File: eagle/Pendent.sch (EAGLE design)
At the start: 25 parts, among them Q1 CMA-4544PF-W, U1 Tiny85-20-SMT, U2 LF50ABDT-TR

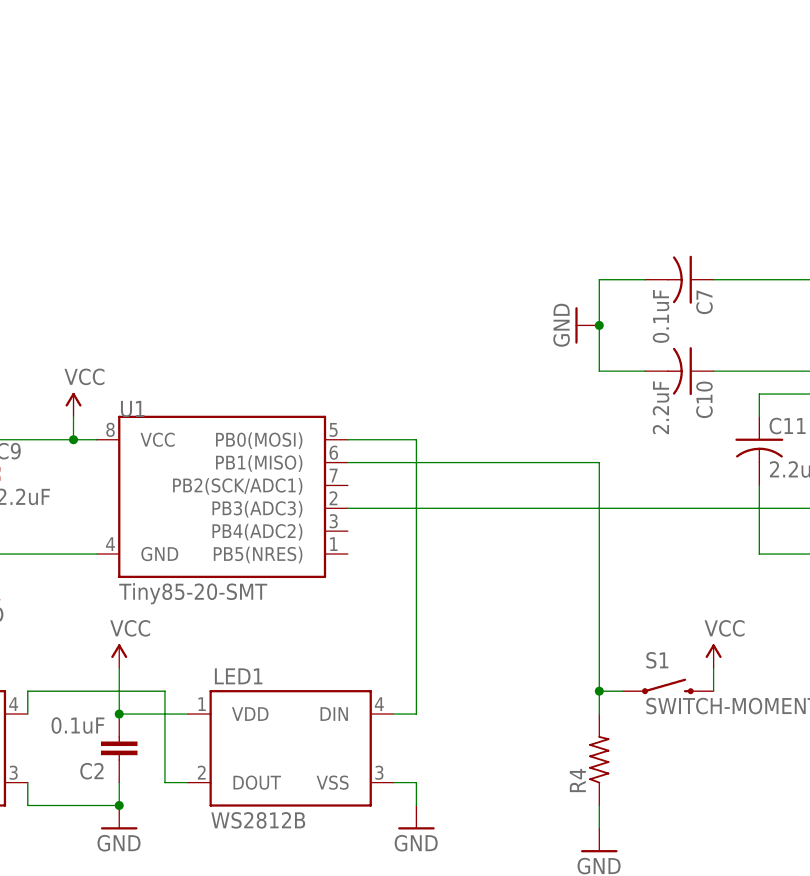
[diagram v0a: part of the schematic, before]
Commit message: Add IRSend add IR LED to schematic
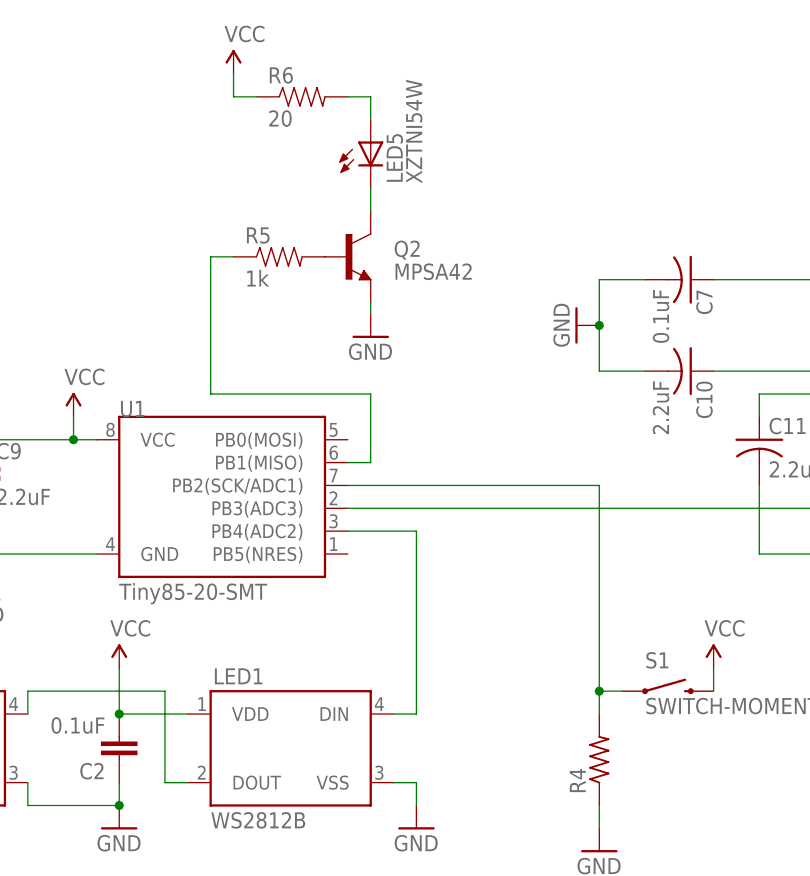
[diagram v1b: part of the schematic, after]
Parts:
- added LED5: XZTNI54W, adafruit:LEDCHIP-LED0805
- added Q2: MPSA42, SparkFun-DiscreteSemi:TRANSISTOR_NPNMPSA42
- added R5: 1k, SparkFun-Passives:RESISTOR0805-RES
- added R6: 20, SparkFun-Passives:RESISTOR0805-RES
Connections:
- new net N$13: Q2.B, R5.2
- new net N$15: LED5.C, Q2.C
- new net N$16: LED5.A, R6.2
- new net N$17: R5.1, U1.PB1(MISO)
- net GND: now also Q2.E
- net N$12: now also U1.PB2(SCK/ADC1); no longer U1.PB1(MISO)
- net N$4: now also U1.PB4(ADC2); no longer U1.PB0(MOSI)
- net VCC: now also R6.1
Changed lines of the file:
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@@
 <part name="GND11" library="SparkFun" deviceset="GND" device=""/>
 <part name="R4" library="adafruit" deviceset="R-US_" device="M0805"/>
+<part name="Q2" library="SparkFun-DiscreteSemi" deviceset="TRANSISTOR_NPN" device="MPSA42" value="MPSA42"/>
+<part name="GND12" library="supply1" deviceset="GND" device=""/>
+<part name="R5" library="SparkFun-Passives" deviceset="RESISTOR" device="0805-RES" value="1k"/>
+<part name="LED5" library="adafruit" deviceset="LED" device="CHIP-LED0805" value="XZTNI54W"/>
+<part name="R6" library="SparkFun-Passives" deviceset="RESISTOR" device="0805-RES" value="20"/>
+<part name="P+8" library="SparkFun" deviceset="VCC" device=""/>
 </parts>
 <sheets>
@@
 <instance part="GND11" gate="1" x="154.94" y="101.6"/>
 <instance part="R4" gate="G$1" x="154.94" y="111.76" rot="R90"/>
+<instance part="Q2" gate="G$1" x="127" y="167.64"/>
+<instance part="GND12" gate="1" x="129.54" y="158.75"/>
+<instance part="R5" gate="G$1" x="119.38" y="167.64"/>
+<instance part="LED5" gate="G$1" x="129.54" y="180.34"/>
+<instance part="R6" gate="G$1" x="121.92" y="185.42"/>
+<instance part="P+8" gate="1" x="114.3" y="187.96"/>
 </instances>
 <busses>
@@
 <pinref part="P+7" gate="1" pin="VCC"/>
 <wire x1="167.64" y1="119.38" x2="167.64" y2="121.92" width="0.1524" layer="91"/>
+</segment>
+<segment>
+<pinref part="P+8" gate="1" pin="VCC"/>
+<wire x1="114.3" y1="187.96" x2="114.3" y2="185.42" width="0.1524" layer="91"/>
+<pinref part="R6" gate="G$1" pin="1"/>
+<wire x1="114.3" y1="185.42" x2="116.84" y2="185.42" width="0.1524" layer="91"/>
 </segment>
 </net>
@@
 <wire x1="154.94" y1="106.68" x2="154.94" y2="104.14" width="0.1524" layer="91"/>
 </segment>
+<segment>
+<pinref part="Q2" gate="G$1" pin="E"/>
+<pinref part="GND12" gate="1" pin="GND"/>
+<wire x1="129.54" y1="161.29" x2="129.54" y2="162.56" width="0.1524" layer="91"/>
+</segment>
 </net>
 <net name="N$1" class="0">
@@
 <net name="N$4" class="0">
 <segment>
-<pinref part="U1" gate="G$1" pin="PB0(MOSI)"/>
-<wire x1="127" y1="147.32" x2="134.62" y2="147.32" width="0.1524" layer="91"/>
-<wire x1="134.62" y1="147.32" x2="134.62" y2="116.84" width="0.1524" layer="91"/>
 <pinref part="LED1" gate="G$1" pin="DIN"/>
+<wire x1="134.62" y1="137.16" x2="134.62" y2="116.84" width="0.1524" layer="91"/>
 <wire x1="134.62" y1="116.84" x2="132.08" y2="116.84" width="0.1524" layer="91"/>
+<pinref part="U1" gate="G$1" pin="PB4(ADC2)"/>
+<wire x1="127" y1="137.16" x2="134.62" y2="137.16" width="0.1524" layer="91"/>
 </segment>
 </net>
@@
 <pinref part="S1" gate="G$1" pin="1"/>
 <wire x1="154.94" y1="119.38" x2="157.48" y2="119.38" width="0.1524" layer="91"/>
-<wire x1="154.94" y1="119.38" x2="154.94" y2="144.78" width="0.1524" layer="91"/>
+<wire x1="154.94" y1="119.38" x2="154.94" y2="142.24" width="0.1524" layer="91"/>
 <junction x="154.94" y="119.38"/>
+<pinref part="U1" gate="G$1" pin="PB2(SCK/ADC1)"/>
+<wire x1="127" y1="142.24" x2="154.94" y2="142.24" width="0.1524" layer="91"/>
+</segment>
+</net>
+<net name="N$13" class="0">
+<segment>
+<pinref part="Q2" gate="G$1" pin="B"/>
+<pinref part="R5" gate="G$1" pin="2"/>
+</segment>
+</net>
+<net name="N$15" class="0">
+<segment>
+<pinref part="Q2" gate="G$1" pin="C"/>
+<pinref part="LED5" gate="G$1" pin="C"/>
+<wire x1="129.54" y1="172.72" x2="129.54" y2="175.26" width="0.1524" layer="91"/>
+</segment>
+</net>
+<net name="N$16" class="0">
+<segment>
+<pinref part="R6" gate="G$1" pin="2"/>
+<wire x1="127" y1="185.42" x2="129.54" y2="185.42" width="0.1524" layer="91"/>
+<pinref part="LED5" gate="G$1" pin="A"/>
+<wire x1="129.54" y1="185.42" x2="129.54" y2="182.88" width="0.1524" layer="91"/>
+</segment>
+</net>
+<net name="N$17" class="0">
+<segment>
 <pinref part="U1" gate="G$1" pin="PB1(MISO)"/>
-<wire x1="154.94" y1="144.78" x2="127" y2="144.78" width="0.1524" layer="91"/>
-</segment>
-</net>
+<wire x1="127" y1="144.78" x2="129.54" y2="144.78" width="0.1524" layer="91"/>
+<wire x1="129.54" y1="144.78" x2="129.54" y2="152.4" width="0.1524" layer="91"/>
+<wire x1="129.54" y1="152.4" x2="111.76" y2="152.4" width="0.1524" layer="91"/>
+<wire x1="111.76" y1="152.4" x2="111.76" y2="167.64" width="0.1524" layer="91"/>
+<pinref part="R5" gate="G$1" pin="1"/>
+<wire x1="111.76" y1="167.64" x2="114.3" y2="167.64" width="0.1524" layer="91"/>
+</segment>
+</net>

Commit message: Board Layout
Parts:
- added JP10: (no value), SparkFun-Connectors:M06SIP
- added R7: 300, adafruit:R-US_M0805
- added S2: SWITCH-MOMENTARY-2SMD-REDUNDANT, SparkFun-Electromechanical:SWITCH-MOMENTARY-2SMD-REDUNDANT
- C2, C3, C4, C5: device SparkFun-Capacitors:0.1UF-25V(+80/-20%)(0603) -> adafruit:C-USC0805K
- C8, C9: device SparkFun-Capacitors:CAP0805 -> adafruit:C-USC0805K
- R4: value (none) -> 10k
- U$3: value (none) -> 6V; device adafruit:CR2032SMT -> SparkFun-Electromechanical:BATTERY20SMD
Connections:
- removed net GAIN: U$1.GAIN
- removed net N$12: R4.2, S1.1, U1.PB2(SCK/ADC1)
- removed net N$17: R5.1, U1.PB1(MISO)
- new net MISO: JP10.3, R5.1, U1.PB1(MISO)
- new net MOSI: JP10.4, U1.PB0(MOSI)
- new net N$18: LED1.DIN, R7.1
- new net RST: JP10.1, S2.1, U1.PB5(NRES)
- new net SCK: JP10.2, R4.2, S1.1, U1.PB2(SCK/ADC1)
- net GND: now also C2.2, C3.2, C4.2, C5.2, JP10.5; no longer C2.1, C3.1, C4.1, C5.1
- net N$2: now also LED2.DOUT
- net N$3: now also LED3.DOUT
- net N$4: now also R7.2; no longer LED1.DIN
- net N$6: no longer U$3.+1
- net VCC: now also C2.1, C3.1, C4.1, C5.1, JP10.6, LED2.VDD, LED3.VDD, LED4.VDD, S2.2, U$1.GAIN; no longer C2.2, C3.2, C4.2, C5.2
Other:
- moved on the sheet: C2, C3, C4, C5, C8, C9, R4, S1

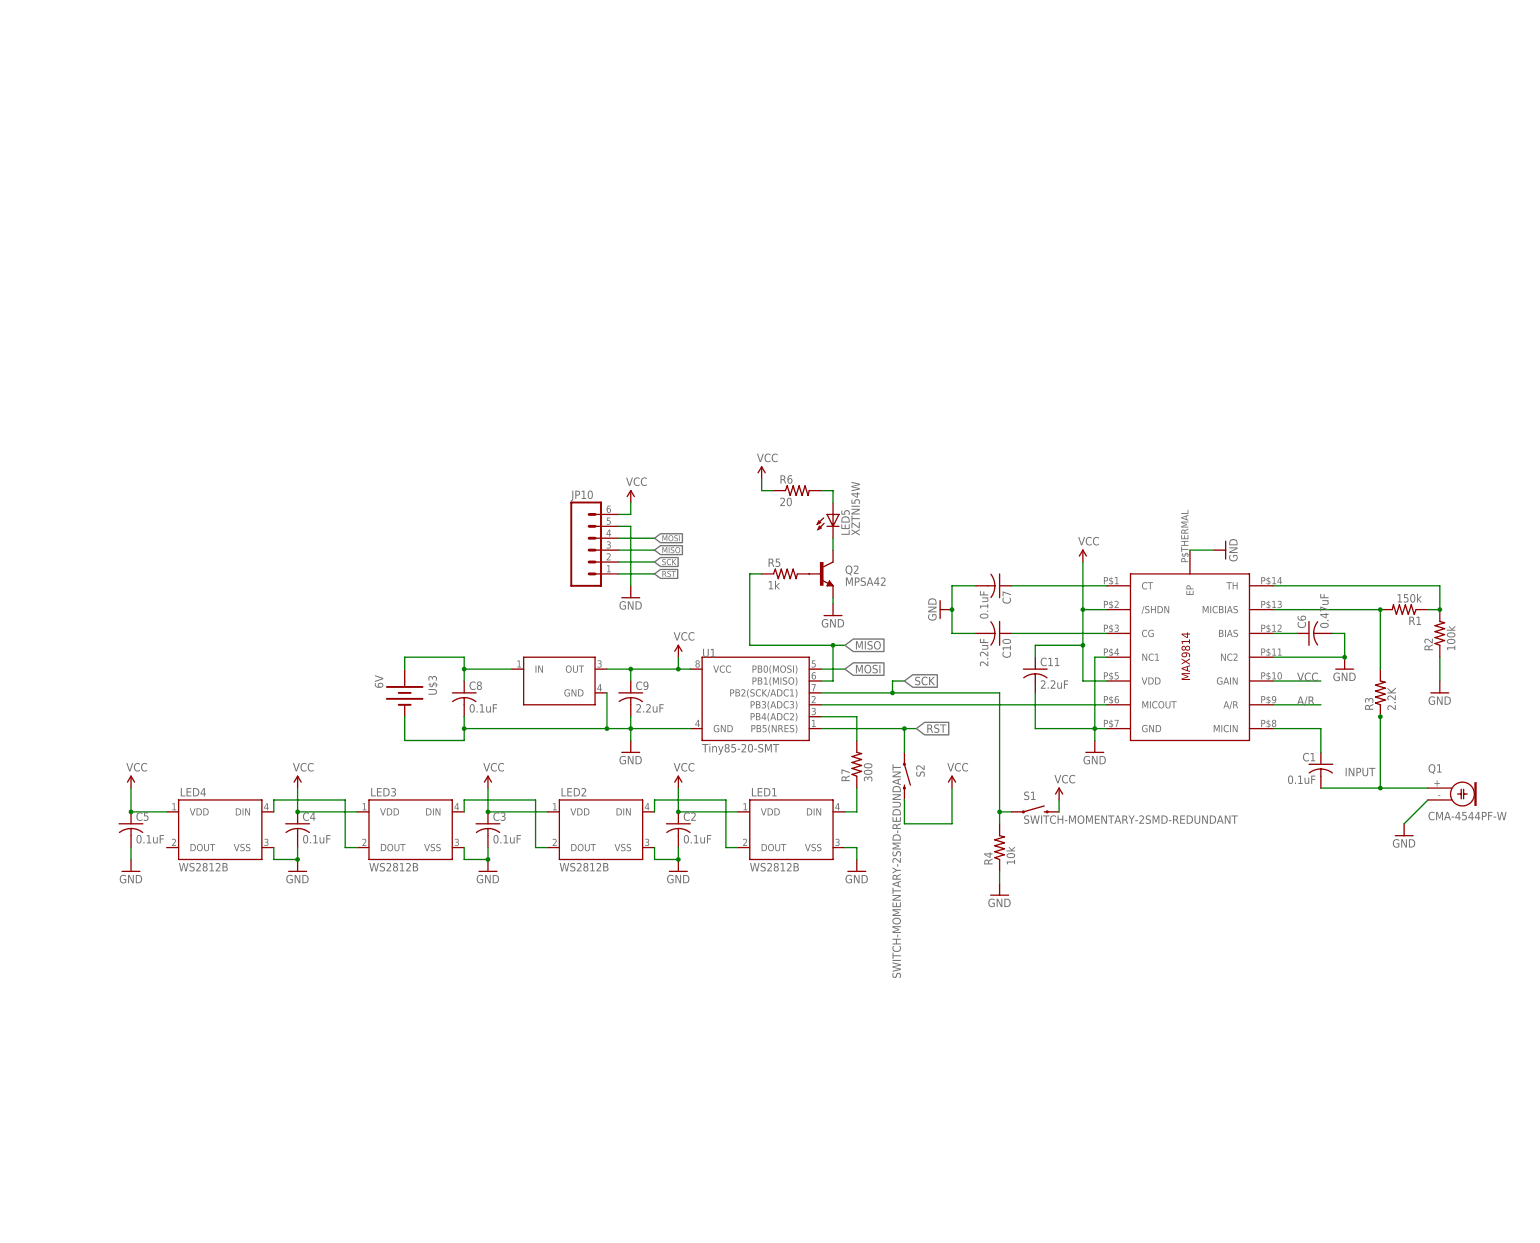
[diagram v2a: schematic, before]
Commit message: Modificaitons to Board to Accomidate ATmega328P-AU
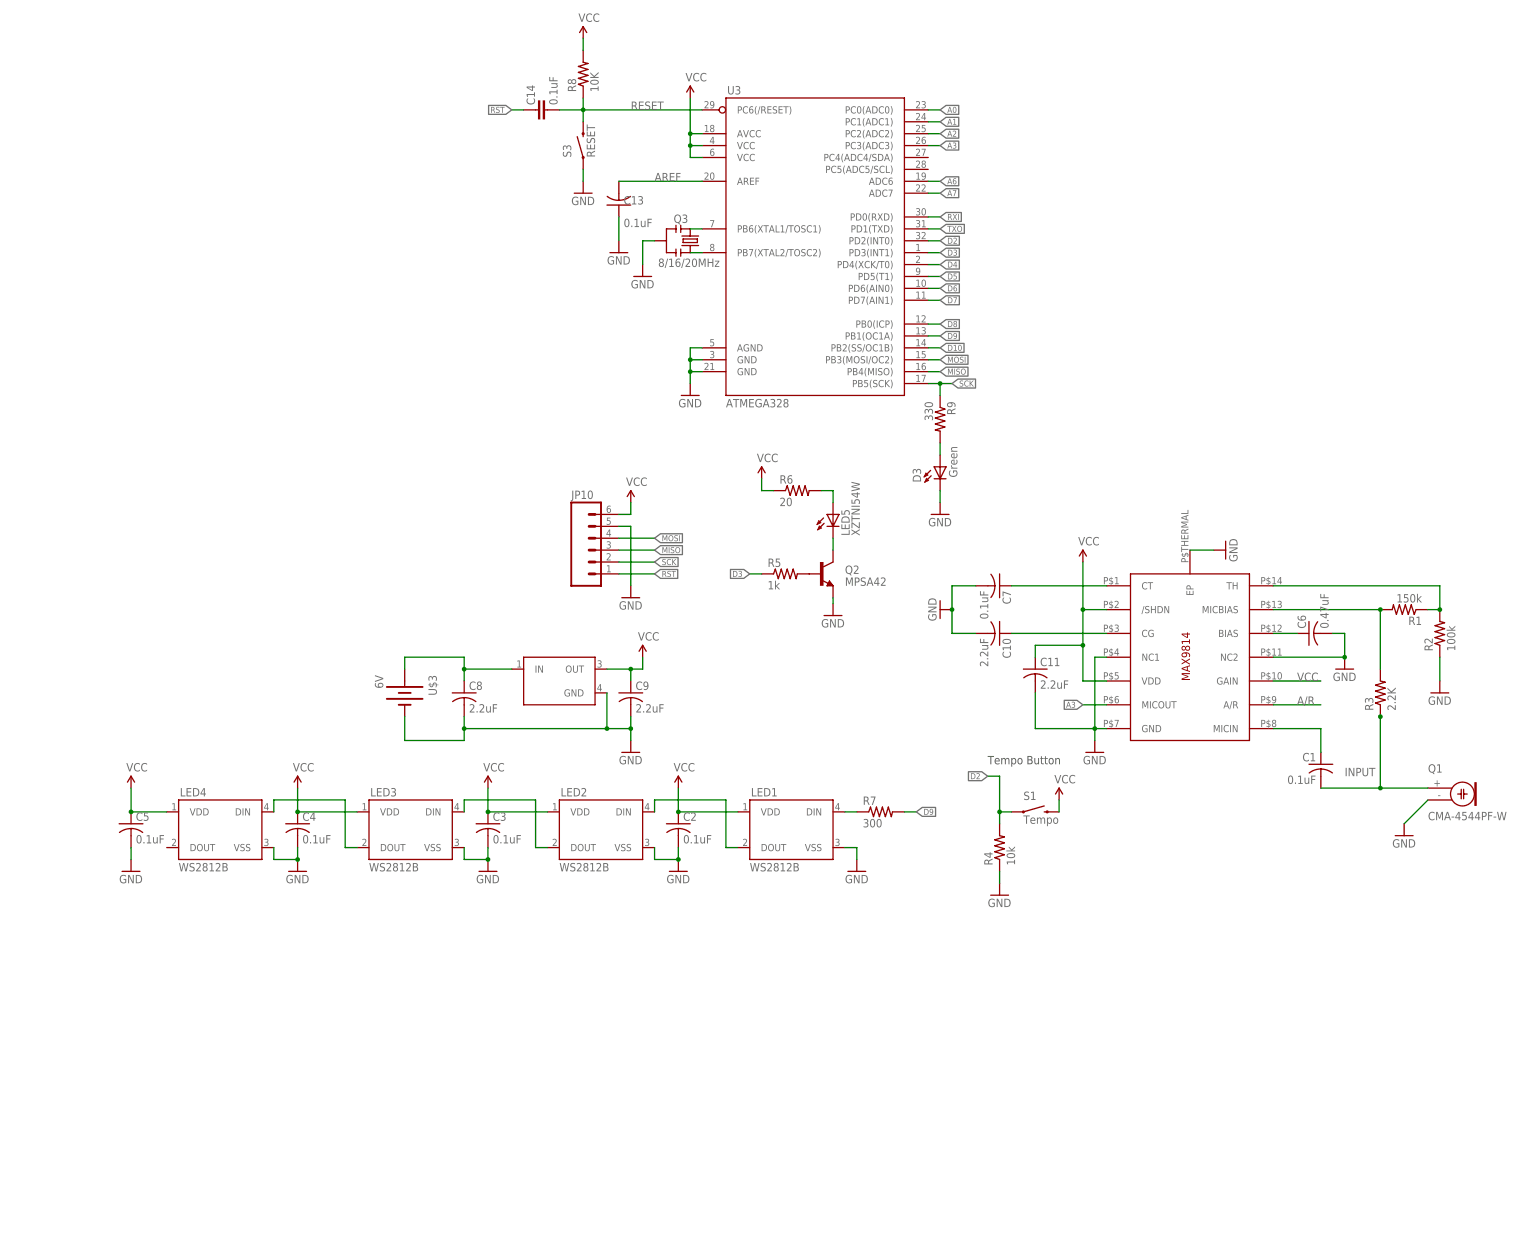
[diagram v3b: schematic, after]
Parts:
- removed S2: SWITCH-MOMENTARY-2SMD-REDUNDANT, SparkFun-Electromechanical:SWITCH-MOMENTARY-2SMD-REDUNDANT
- removed U$1: MAX9814TDFN14, adafruit:MAX9814TDFN14
- added C13: 0.1uF, adafruit:C-USC0805K
- added C14: 0.1uF, SparkFun:CAP0603-CAP
- added D3: Green, adafruit:LEDCHIPLED_0805
- added Q3: 8/16/20MHz, Testing:RESONATOR1:1
- added R8: 10K, adafruit:R-US_R0805
- added R9: 330, adafruit:R-US_R0805
- added S3: RESET, Testing:SWITCH-MOMENTARY-2SMD-ALT01
- added U3: ATMEGA328, SparkFun:ATMEGA168
- C8: value 0.1uF -> 2.2uF
- R4, R7: device adafruit:R-US_M0805 -> adafruit:R-US_R0805
- R5, R6: device SparkFun-Passives:RESISTOR0805-RES -> adafruit:R-US_R0805
- S1: value SWITCH-MOMENTARY-2SMD-REDUNDANT -> Tempo
- U1: value Tiny85-20-SMT -> MAX9814TDFN14; device SparkFun-DigitalIC:ATTINY45TINY85-20-SMT -> adafruit:MAX9814TDFN14
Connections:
- net N$6 renamed VBATT
- removed net N$14: U$1.MICOUT, U1.PB3(ADC3)
- removed net N$4: R7.2, U1.PB4(ADC2)
- new net A0: U3.PC0(ADC0)
- new net A1: U3.PC1(ADC1)
- new net A2: U3.PC2(ADC2)
- new net A3: U1.MICOUT, U3.PC3(ADC3)
- new net A6: U3.ADC6
- new net A7: U3.ADC7
- new net AREF: C13.2, U3.AREF
- new net D10: U3.PB2(SS/OC1B)
- new net D2: R4.2, S1.1, U3.PD2(INT0)
- new net D3: R5.1, U3.PD3(INT1)
- new net D4: U3.PD4(XCK/T0)
- new net D5: U3.PD5(T1)
- new net D6: U3.PD6(AIN0)
- new net D7: U3.PD7(AIN1)
- new net D8: U3.PB0(ICP)
- new net D9: R7.2, U3.PB1(OC1A)
- new net N$1: D3.A, R9.2
- new net N$12: Q3.3, U3.PB7(XTAL2/TOSC2)
- new net N$17: Q3.1, U3.PB6(XTAL1/TOSC1)
- new net RESET: C14.1, R8.1, S3.2, U3.PC6(/RESET)
- new net RXI: U3.PD0(RXD)
- new net TXO: U3.PD1(TXD)
- net A/R: now also U1.A/R; no longer U$1.A/R
- net GND: now also C13.1, D3.C, Q3.2, S3.1, U1.EP, U1.NC1, U1.NC2, U3.AGND, U3.GND@1, U3.GND@2; no longer U$1.EP, U$1.GND, U$1.NC1, U$1.NC2
- net MISO: now also U3.PB4(MISO); no longer R5.1, U1.PB1(MISO)
- net MOSI: now also U3.PB3(MOSI/OC2); no longer U1.PB0(MOSI)
- net N$10: now also U1.TH; no longer U$1.TH
- net N$11: now also U1.MICBIAS; no longer U$1.MICBIAS
- net N$5: now also U1.MICIN; no longer U$1.MICIN
- net N$7: now also U1.BIAS; no longer U$1.BIAS
- net N$8: now also U1.CT; no longer U$1.CT
- net N$9: now also U1.CG; no longer U$1.CG
- net RST: now also C14.2; no longer S2.1, U1.PB5(NRES)
- net SCK: now also R9.1, U3.PB5(SCK); no longer R4.2, S1.1, U1.PB2(SCK/ADC1)
- net VCC: now also R8.2, U1./SHDN, U1.GAIN, U1.VDD, U3.AVCC, U3.VCC@1, U3.VCC@2; no longer S2.2, U$1./SHDN, U$1.GAIN, U$1.VDD, U1.VCC
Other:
- note added: "Tempo Button"
- moved on the sheet: R7
